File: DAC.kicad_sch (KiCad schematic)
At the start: 81 parts, among them IC1 74682N, IC19 74153N, IC3 74LS08N, IC4 74153N, J1 DE15_Receptacle_HighDensity, J2 Conn_02x20_Odd_Even, J3 Conn_02x10_Odd_Even, Q1 17.734475MHz, U1 74AS574, U10 LM34Z, U11 74AS574, U12 74ALS137, U13 74ALS137, U14 74LS393, U15 74LS74, U16 74LS153, U17 74LS11, U18 74LS00, U19 74LS32, U2 74LS153, U20 74LS139, U21 74LS10, U22 74LS125, U26 74LS175, U3 74F04, U4 74F86, U5 74F161, U6 74LS04, U7 74ALS574, U8 74LS590, U9 74LS590

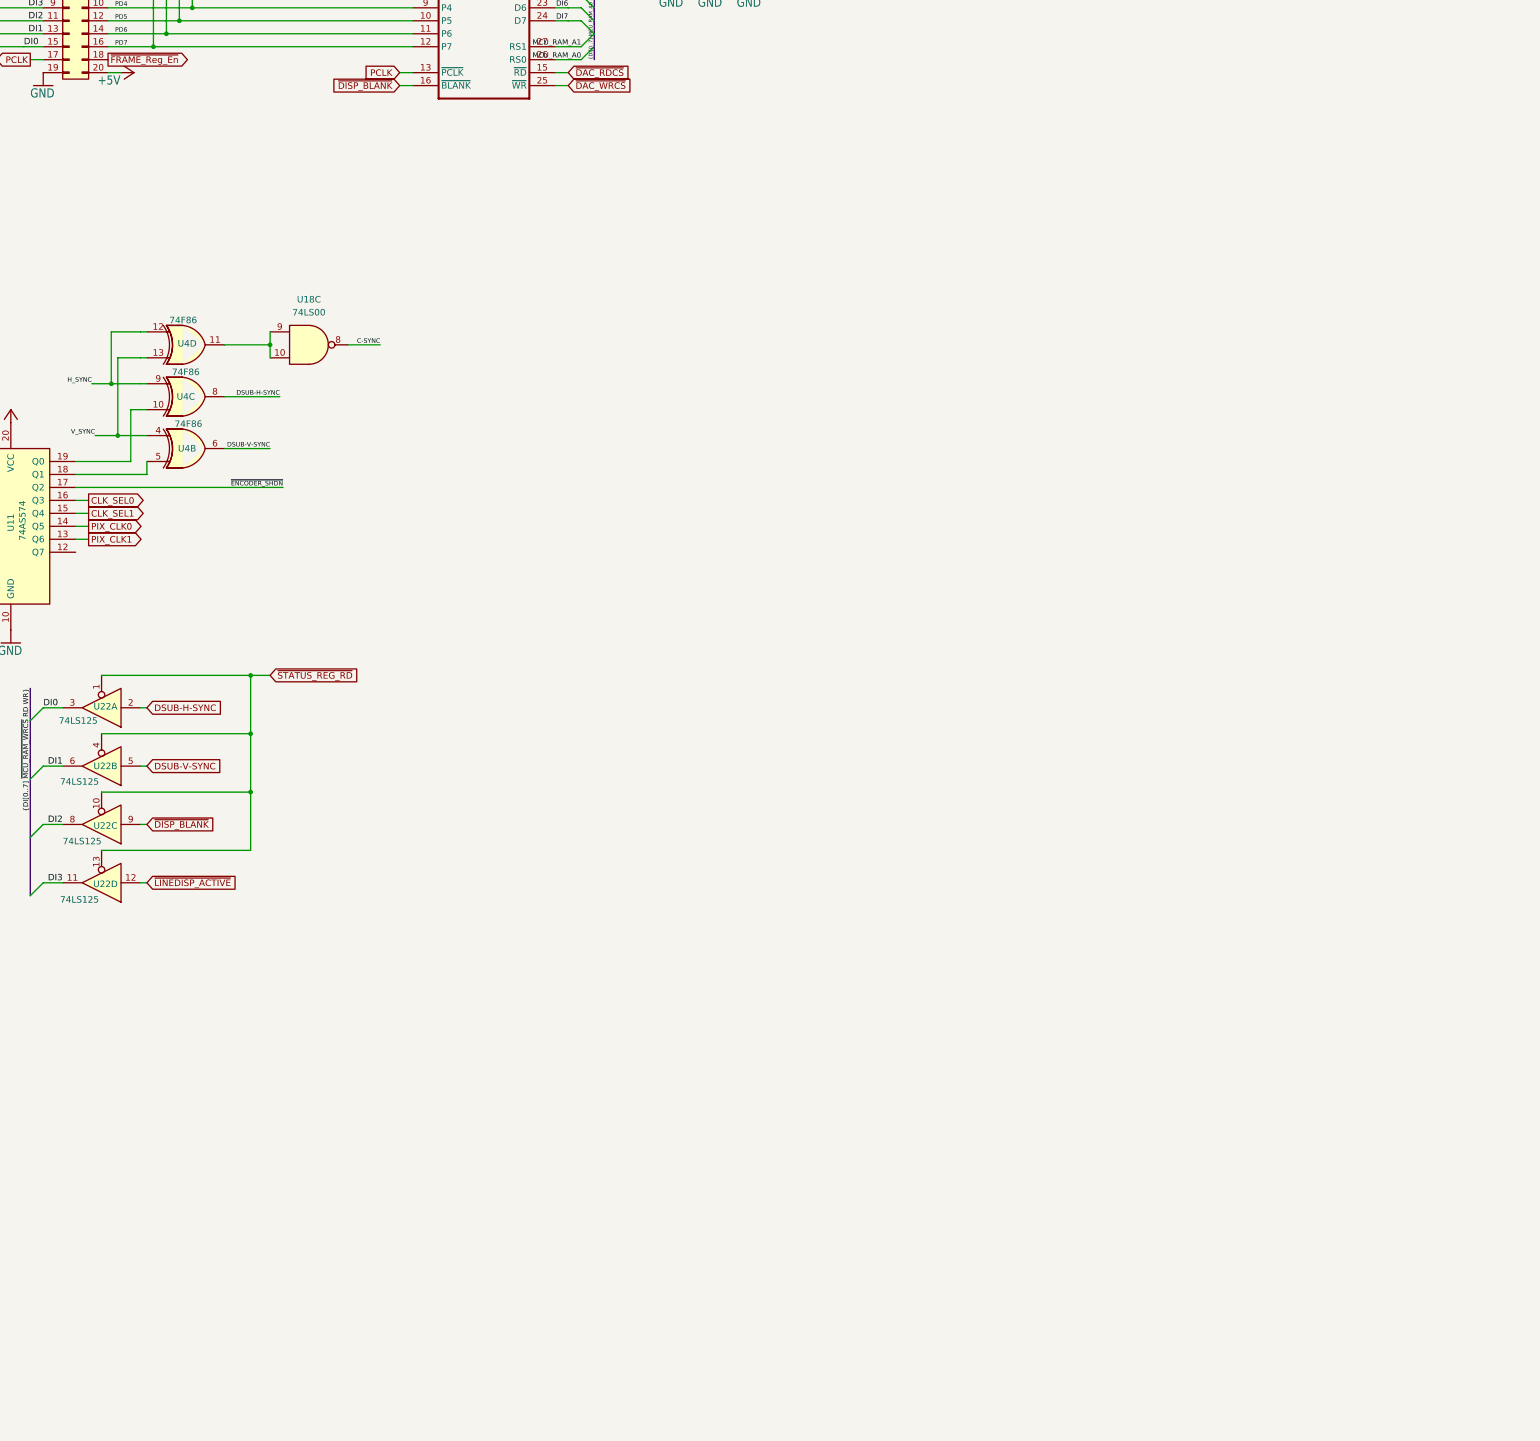
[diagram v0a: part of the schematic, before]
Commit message: Add files via upload
Complete schematics of working graphics adapter.
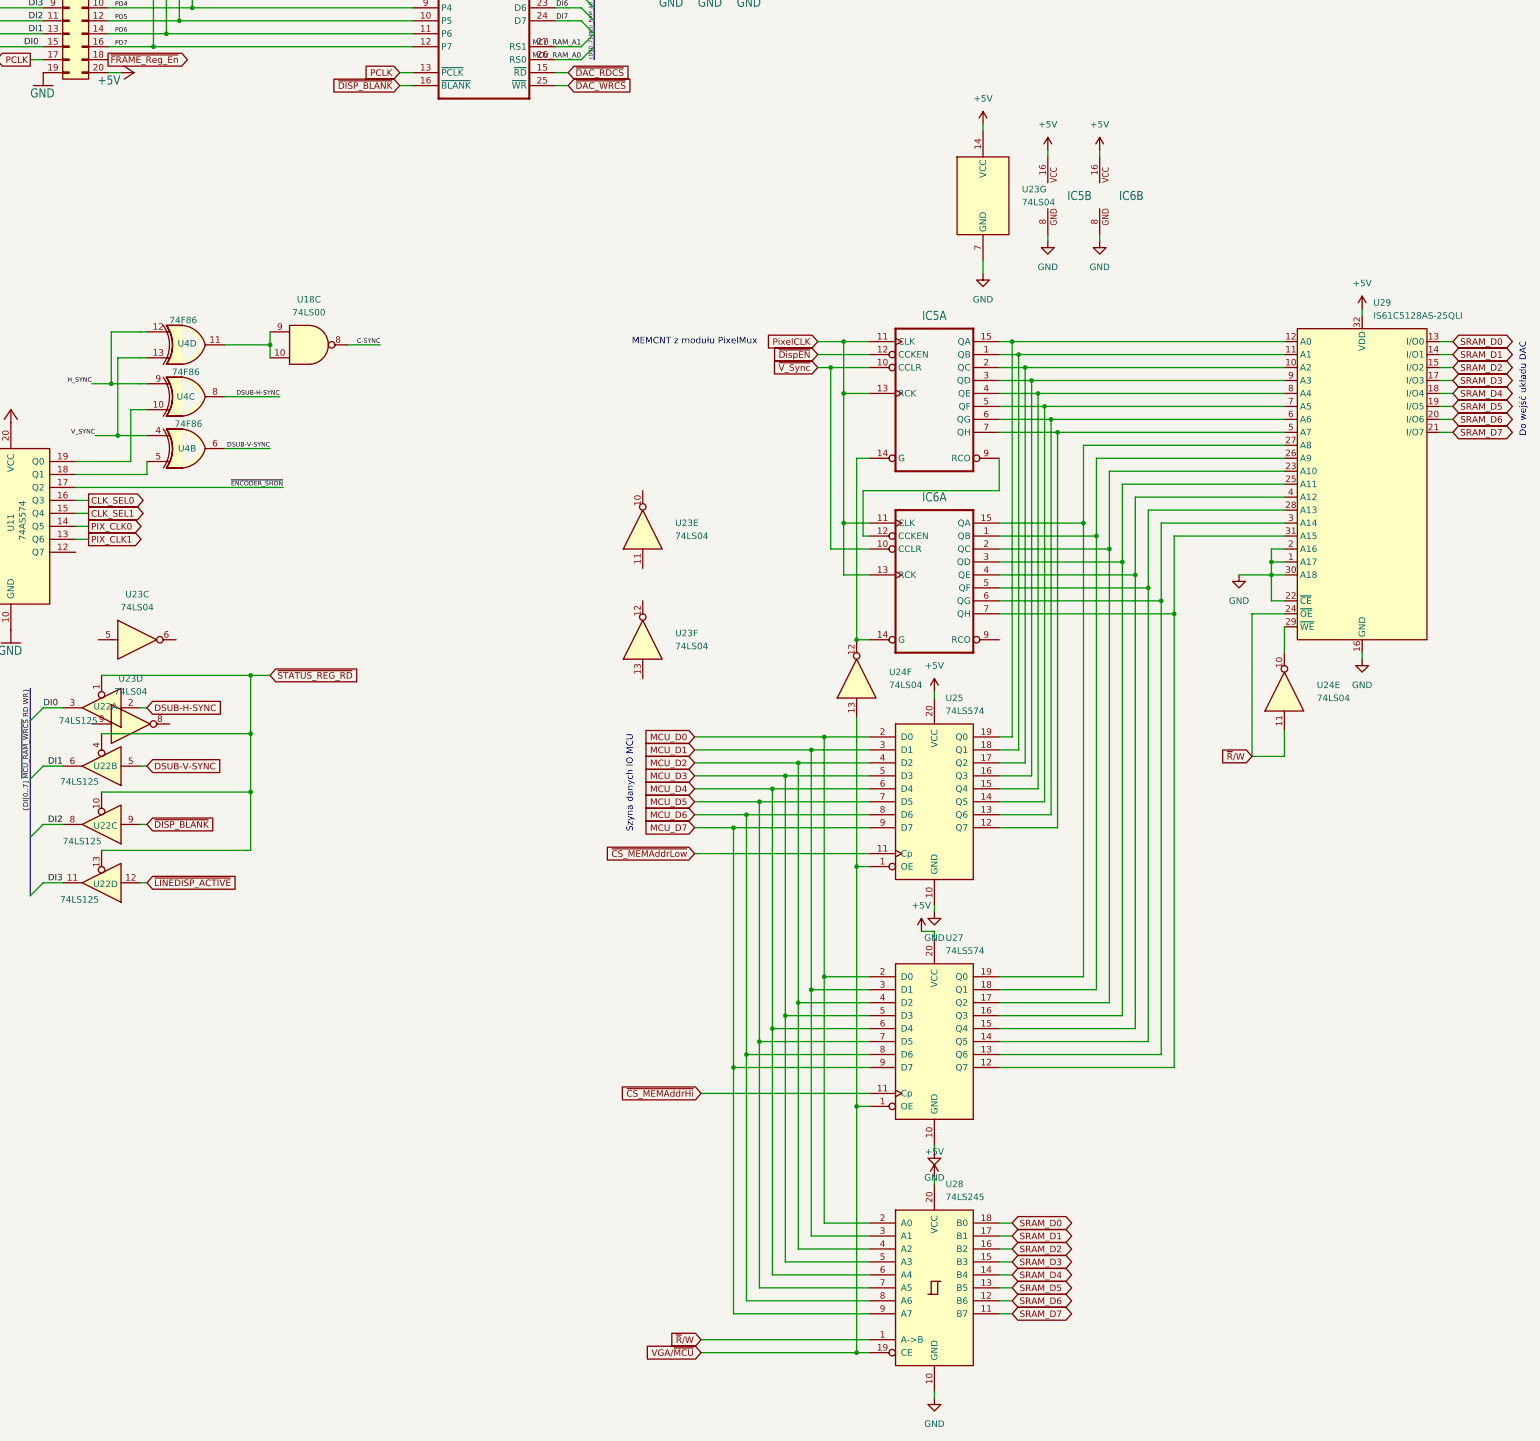
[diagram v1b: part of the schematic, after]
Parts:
- added IC5, IC6: ~, HV-Syncsch:SO16, symbol HV-Syncsch-eagle-import:74590D
- added U23, U24: 74LS04, symbol 74xx:74LS04
- added U25, U27: 74LS574, symbol 74xx:74LS574
- added U28: 74LS245, symbol 74xx:74LS245
- added U29: IS61C5128AS-25QLI, Package_SO:SSOP-32_11.305x20.495mm_P1.27mm, symbol Memory_RAM:IS61C5128AS-25QLI
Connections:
- net +5V: now also IC5.16 (VCC), IC6.16 (VCC), U23.14 (VCC), U25.20 (VCC), U27.20 (VCC), U28.20 (VCC), U29.32 (VDD)
- net GND: now also IC5.8 (GND), IC6.8 (GND), U23.7 (GND), U25.10 (GND), U27.10 (GND), U28.10 (GND), U29.1 (A17), U29.16 (GND), U29.2 (A16), U29.22 (~{CE}), U29.30 (A18)
- new net: IC5.14 (G), IC6.14 (G), U24.12
- new net: IC5.2 (QC), U25.17 (Q2), U29.10 (A2)
- new net: IC5.1 (QB), U25.18 (Q1), U29.11 (A1)
- new net: IC5.15 (QA), U25.19 (Q0), U29.12 (A0)
- new net: IC6.2 (QC), U27.17 (Q2), U29.23 (A10)
- new net: IC6.3 (QD), U27.16 (Q3), U29.25 (A11)
- new net: IC6.1 (QB), U27.18 (Q1), U29.26 (A9)
- new net: IC6.15 (QA), U27.19 (Q0), U29.27 (A8)
- new net: IC6.5 (QF), U27.14 (Q5), U29.28 (A13)
- new net: U24.10, U29.29 (~{WE})
- new net: IC6.6 (QG), U27.13 (Q6), U29.3 (A14)
- new net: IC6.7 (QH), U27.12 (Q7), U29.31 (A15)
- new net: IC6.4 (QE), U27.15 (Q4), U29.4 (A12)
- new net: IC5.7 (QH), U25.12 (Q7), U29.5 (A7)
- new net: IC5.6 (QG), U25.13 (Q6), U29.6 (A6)
- new net: IC5.5 (QF), U25.14 (Q5), U29.7 (A5)
- new net: IC5.4 (QE), U25.15 (Q4), U29.8 (A4)
- new net: IC5.3 (QD), U25.16 (Q3), U29.9 (A3)
- new net: IC5.9 (RCO), IC6.12 (CCKEN)
- new net MCU_D0: U25.2 (D0), U27.2 (D0), U28.2 (A0)
- new net MCU_D1: U25.3 (D1), U27.3 (D1), U28.3 (A1)
- new net MCU_D2: U25.4 (D2), U27.4 (D2), U28.4 (A2)
- new net MCU_D3: U25.5 (D3), U27.5 (D3), U28.5 (A3)
- new net MCU_D4: U25.6 (D4), U27.6 (D4), U28.6 (A4)
- new net MCU_D5: U25.7 (D5), U27.7 (D5), U28.7 (A5)
- new net MCU_D6: U25.8 (D6), U27.8 (D6), U28.8 (A6)
- new net MCU_D7: U25.9 (D7), U27.9 (D7), U28.9 (A7)
- new net PixelCLK: IC5.11 (CLK), IC5.13 (RCK), IC6.11 (CLK), IC6.13 (RCK)
- new net SRAM_D0: U28.18 (B0), U29.13 (I/O0)
- new net SRAM_D1: U28.17 (B1), U29.14 (I/O1)
- new net SRAM_D2: U28.16 (B2), U29.15 (I/O2)
- new net SRAM_D3: U28.15 (B3), U29.17 (I/O3)
- new net SRAM_D4: U28.14 (B4), U29.18 (I/O4)
- new net SRAM_D5: U28.13 (B5), U29.19 (I/O5)
- new net SRAM_D6: U28.12 (B6), U29.20 (I/O6)
- new net SRAM_D7: U28.11 (B7), U29.21 (I/O7)
- new net VGA/~{MCU}: U24.13, U25.1 (OE), U27.1 (OE), U28.19 (CE)
- new net ~{CS_MEMAddrHi}: U27.11 (Cp)
- new net ~{CS_MEMAddrLow}: U25.11 (Cp)
- new net ~{DispEN}: IC5.12 (CCKEN)
- new net ~{R}/W: U24.11, U28.1 (A->B), U29.24 (~{OE})
- new net ~{V_Sync}: IC5.10 (CCLR), IC6.10 (CCLR)
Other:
- note added: "Do wejść układu DAC"
- note added: "MEMCNT z modułu PixelMux"
- note added: "Szyna danych IO MCU"
